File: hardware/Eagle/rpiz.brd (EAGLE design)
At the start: 67.3 x 28.9 mm, 19 parts, among them Q1 2N5484, Q2 2N5484

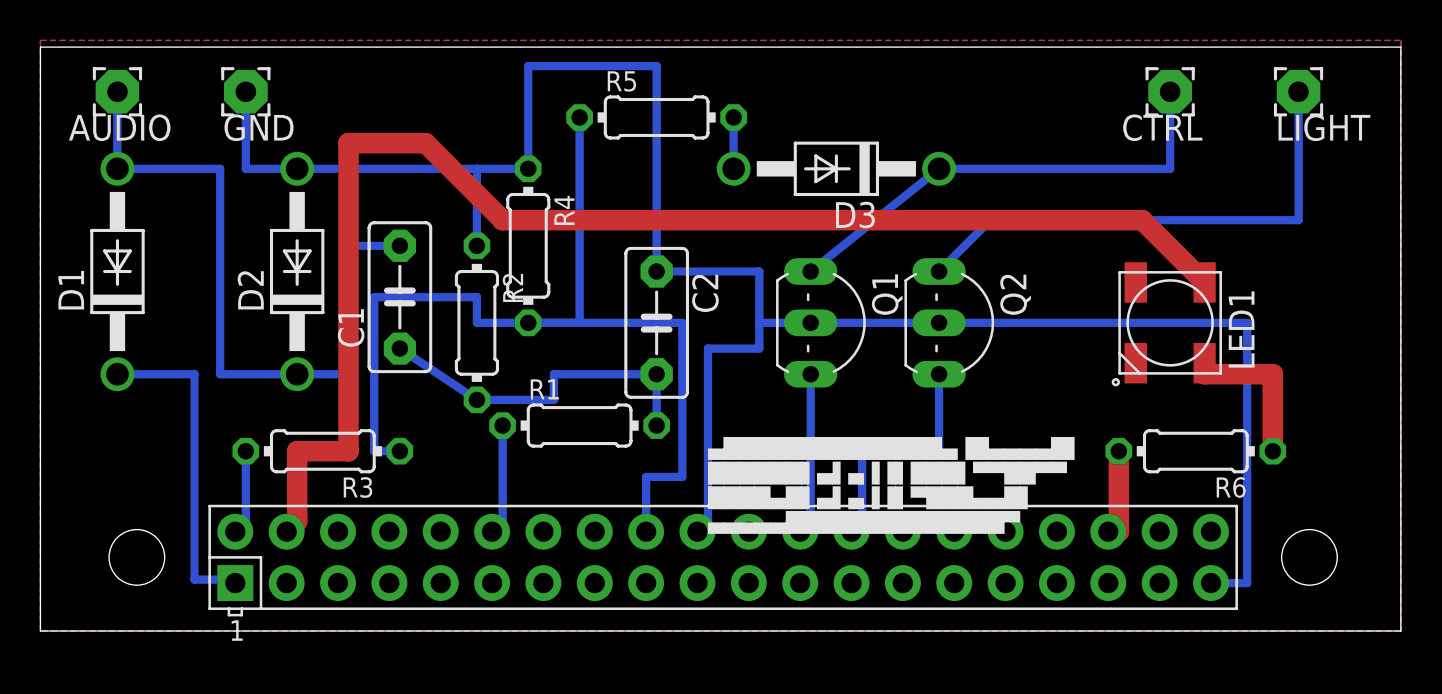
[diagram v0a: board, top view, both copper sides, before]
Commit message: board is now using 2n7000 mosfet, also added 2nd LED
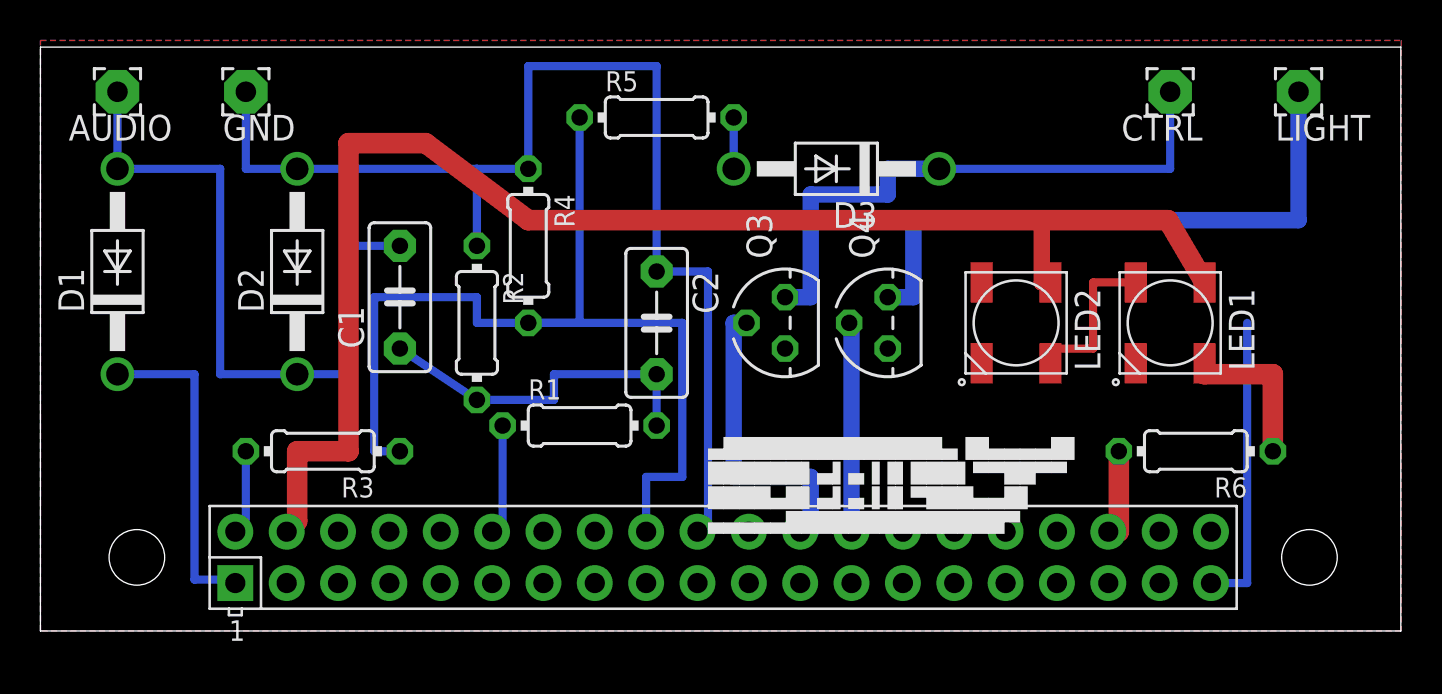
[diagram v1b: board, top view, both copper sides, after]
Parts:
- removed Q1, Q2: 2N5484, transistor-fet:TO92-
- added LED2: WS2812B, WS2812B:WS2812B
- added Q3, Q4: (no value), transistors:TO-92
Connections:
- new net N$11: LED1.DOUT, LED2.DIN
- net 5V0@2: now also LED2.VDD
- net GND: now also LED2.VSS, Q3.1, Q4.1; no longer Q1.2, Q2.2
- net N$2: now also Q3.3; no longer Q1.3
- net N$3: now also Q3.2; no longer Q1.1
- net N$7: now also Q4.2; no longer Q2.1
- net N$9: now also Q4.3; no longer Q2.3
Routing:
- net GND: track 103.1 -> 73.9 mm
- net N$11: track 0.00 -> 8.22 mm
- net N$3: track 8.31 -> 15.3 mm
- net N$2: track 23.4 -> 29.2 mm
- net N$9: track 25.2 -> 30.5 mm
- net 5V0@2: track 67.2 -> 70.9 mm
- net N$7: track 12.1 -> 11.0 mm
